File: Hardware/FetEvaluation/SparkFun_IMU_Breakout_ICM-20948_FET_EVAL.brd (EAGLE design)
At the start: 25.4 x 25.4 mm, 102 parts, among them Q1 DMN2005LP4K-7, Q10 RE1C002UN, Q11 DMN2005LP4K-7, Q12 RE1C002UN, Q13 DMN2005LP4K-7, Q14 RE1C002UN, Q15 DMN2005LP4K-7, Q16 RE1C002UN, Q2 RE1C002UN, Q3 DMN2005LP4K-7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

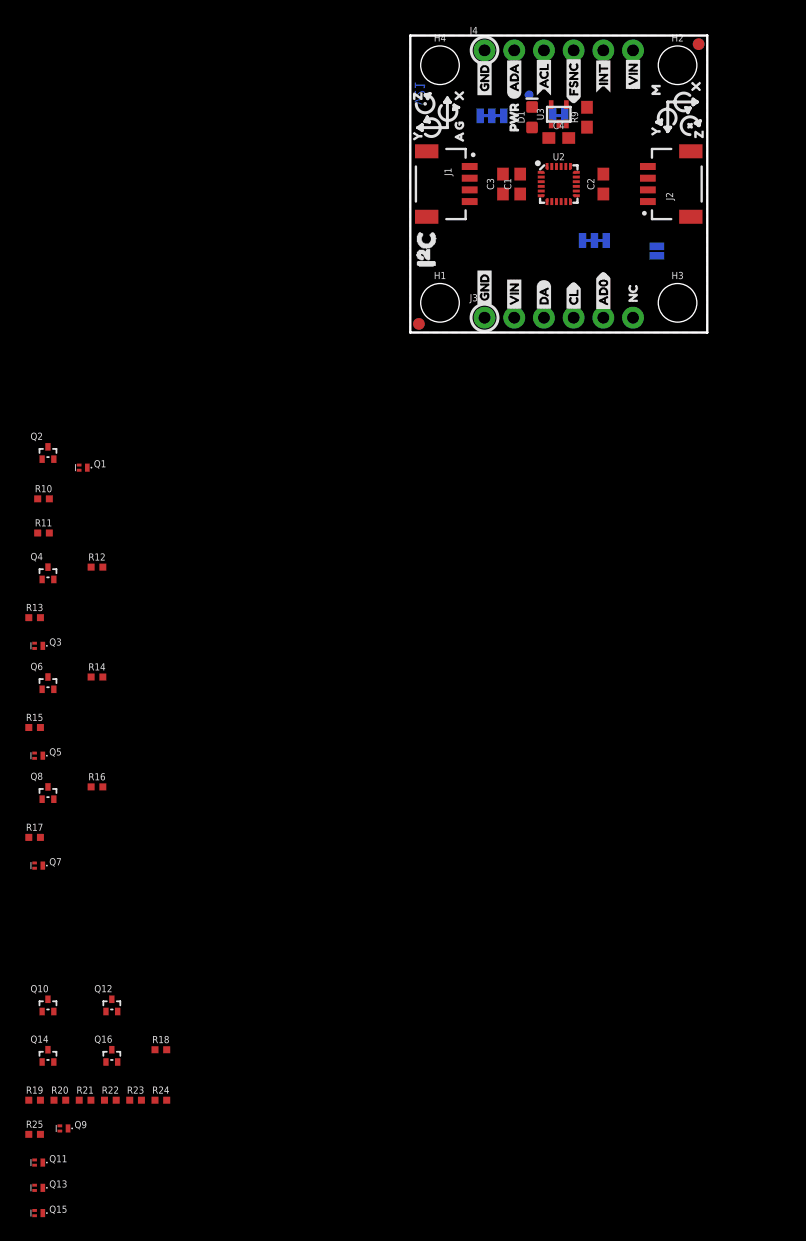
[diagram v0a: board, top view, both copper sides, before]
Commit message: Laid out board for MOSFET trick evaluation (prototype)
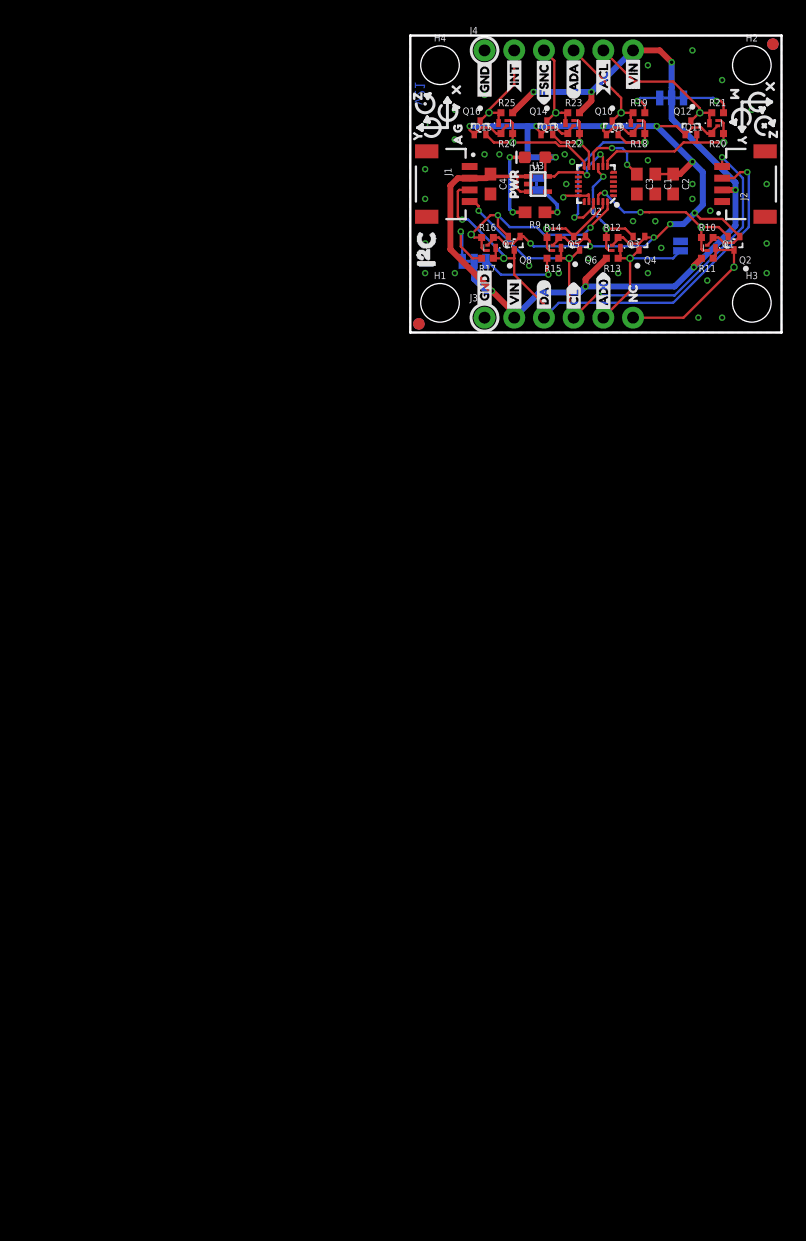
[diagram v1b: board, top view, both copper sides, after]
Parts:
- added U1, U10, U11, U12, U13, U14, U15, U16, U17, U18, U4, U5, U6, U7, U8, U9: TP, new_fets:MINI_TEST_POINT
- moved Q11 106.4 mm to (26.3, 17.9), turned to 180 degrees
- moved Q13 102.1 mm to (14.0, 17.9), turned to 180 degrees
- moved Q15 101.6 mm to (8.26, 17.9), turned to 180 degrees
- moved R21 100.3 mm to (26.3, 18.8)
- moved R20 100.0 mm to (26.3, 17.0), turned to 180 degrees
- moved Q9 99.2 mm to (19.6, 17.9), turned to 180 degrees
- moved R19 99.0 mm to (19.6, 18.8)
- moved R25 96.3 mm to (8.26, 18.8)
- moved R23 92.4 mm to (14.0, 18.8)
- moved R22 91.7 mm to (14.0, 17.0), turned to 180 degrees
- moved Q14 90.1 mm to (11.7, 18.0)
- moved Q12 89.9 mm to (24.0, 18.0)
- moved Q10 89.2 mm to (17.3, 18.0)
- moved R18 88.4 mm to (19.6, 17.0), turned to 180 degrees
- moved R24 87.8 mm to (8.26, 17.0), turned to 180 degrees
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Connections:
- net !CS: now also U17.P$1
- net !CS!_VIN: now also U18.P$1
- net AD0/SDO: now also U15.P$1
- net AD0/SDO_VIN: now also U16.P$1
- net AUX_CL: now also U5.P$1
- net AUX_CL_VIN: now also J4.5, U6.P$1; no longer J4.3
- net AUX_DA: now also U1.P$1
- net AUX_DA_VIN: now also J4.4, U4.P$1; no longer J4.2
- net FSYNC: now also U8.P$1
- net FSYNC_VIN: now also J4.3, U7.P$1; no longer J4.4
- net INT: now also U9.P$1
- net INT_VIN: now also J4.2, U10.P$1; no longer J4.5
- net SCL/SCLK: now also U13.P$1
- net SCL/SCLK_VIN: now also U14.P$1
- net SDA/SDI: now also U11.P$1
- net SDA/SDI_VIN: now also U12.P$1
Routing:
- net 1.8V: track 0.00 -> 100.8 mm, vias 0 -> 13
- net VIN: track 0.00 -> 88.5 mm, vias 0 -> 7
- net SDA/SDI_VIN: track 0.00 -> 46.5 mm, vias 0 -> 2
- net SCL/SCLK_VIN: track 0.00 -> 44.2 mm, vias 0 -> 3
- net SDA/SDI: track 0.00 -> 19.3 mm, vias 0 -> 2
- net AUX_DA: track 0.00 -> 18.4 mm, vias 0 -> 1
- net !CS: track 0.00 -> 15.7 mm, vias 0 -> 2
- net !CS!_VIN: track 0.00 -> 14.5 mm
- net AUX_CL: track 0.00 -> 14.0 mm
- net AUX_CL_VIN: track 0.00 -> 13.7 mm
- net AD0/SDO_VIN: track 0.00 -> 13.7 mm
- net INT: track 0.00 -> 12.0 mm
- net AD0/SDO: track 0.00 -> 11.2 mm, vias 0 -> 1
- net AUX_DA_VIN: track 0.00 -> 10.1 mm
- net INT_VIN: track 0.00 -> 9.28 mm
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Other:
- board size 25.4 x 25.4 mm -> 31.8 x 25.4 mm

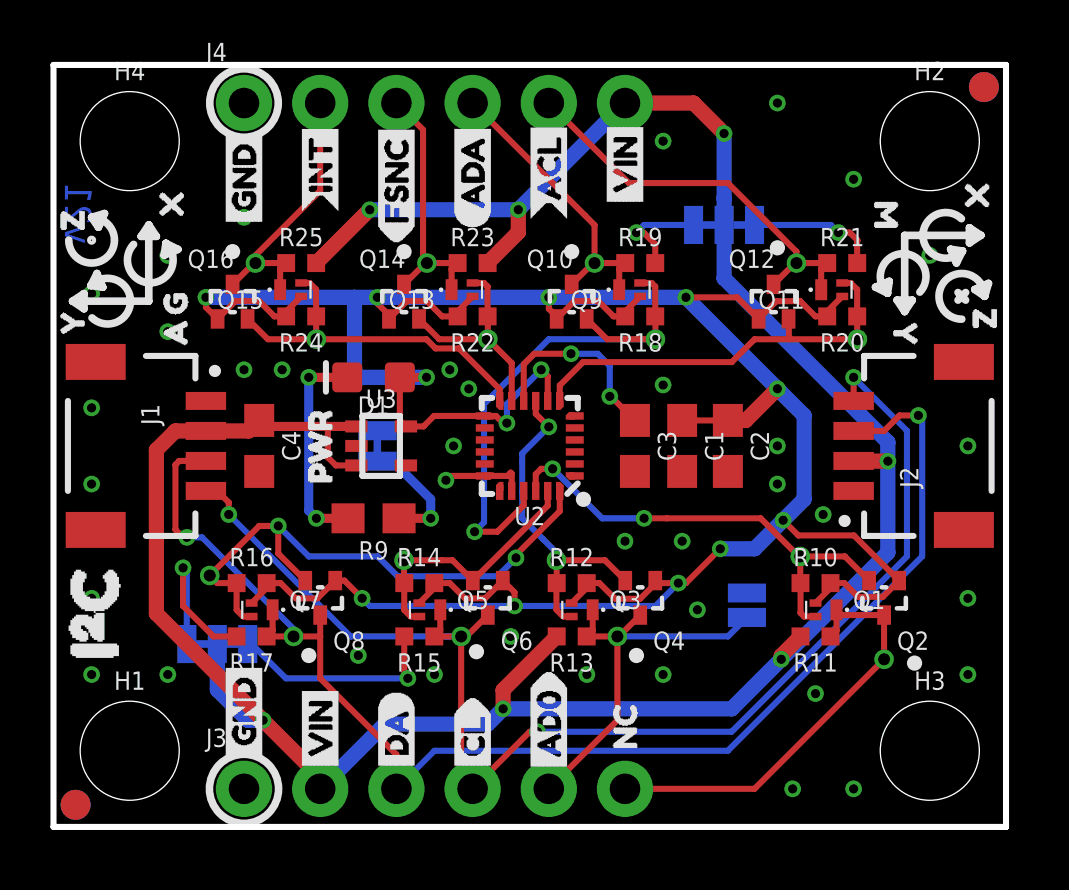
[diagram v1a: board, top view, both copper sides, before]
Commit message: Updated test point package with keepout
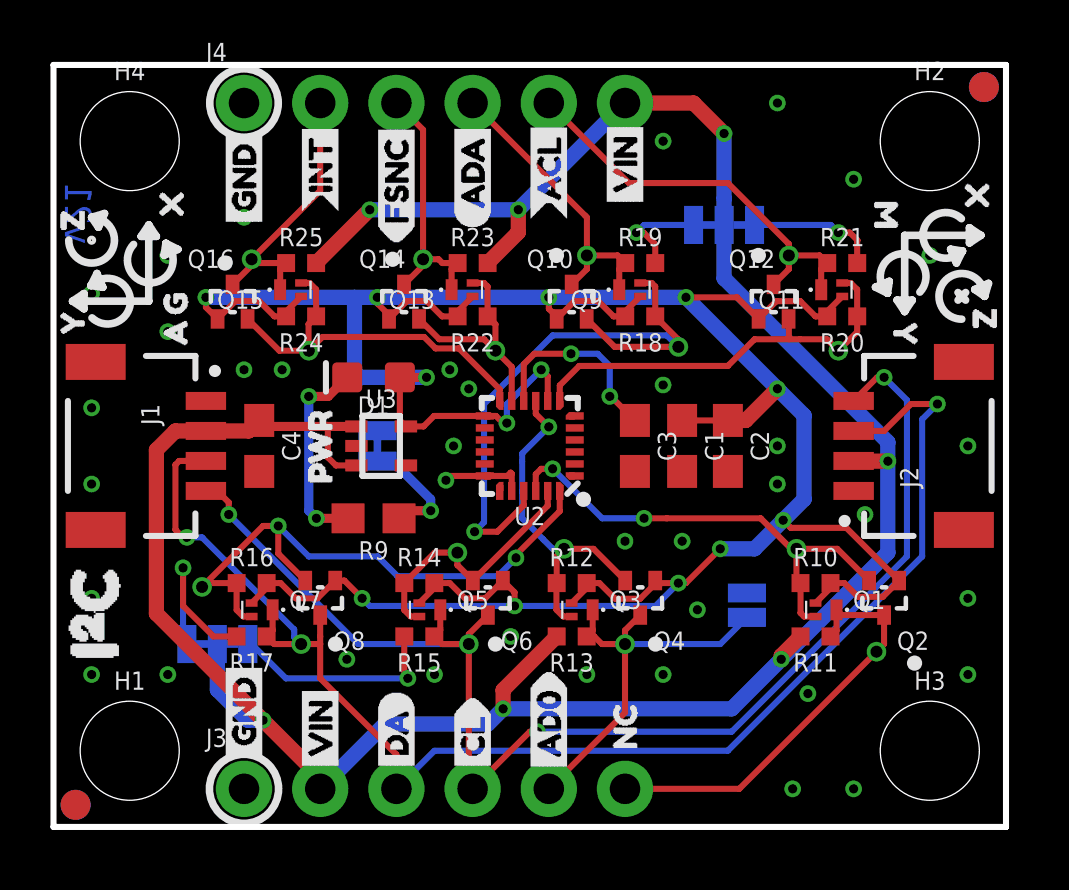
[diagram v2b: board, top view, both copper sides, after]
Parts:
- moved U13 1.80 mm to (13.5, 9.14)
- moved U1 0.80 mm to (20.8, 16.0)
- moved U5 0.74 mm to (26.2, 15.9)
- moved U15 0.46 mm to (17.0, 9.27)
- moved U11 0.46 mm to (4.95, 8.00)
- moved U8 0.46 mm to (14.7, 15.9)
- moved U9 0.46 mm to (8.51, 15.9)
- moved U6 0.36 mm to (24.5, 19.1)
- moved U12 0.36 mm to (8.26, 6.10)
- moved U16 0.36 mm to (19.1, 6.10)
- moved U18 0.36 mm to (27.4, 5.84)
- moved U14 0.36 mm to (13.8, 6.10)
- moved U4 0.36 mm to (17.8, 19.1)
- moved U17 0.28 mm to (24.8, 9.27)
- moved U10 0.18 mm to (6.60, 18.9)
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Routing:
- net AUX_DA: track 18.4 -> 20.8 mm
- net SDA/SDI_VIN: track 46.5 -> 48.1 mm
- net INT: track 12.0 -> 12.8 mm
- net SDA/SDI: track 19.3 -> 19.9 mm
- net SCL/SCLK_VIN: track 44.2 -> 44.8 mm

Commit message: Commit for design review
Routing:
- net SDA/SDI_VIN_JMP: track 6.07 -> 4.76 mm
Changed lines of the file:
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@@
 <contactref element="R17" pad="2"/>
 <contactref element="JP4" pad="1"/>
-<wire x1="4.318" y1="7.366" x2="5.334" y2="6.35" width="0.2032" layer="1"/>
-<via x="4.318" y="8.636" extent="1-16" drill="0.3048"/>
-<wire x1="4.318" y1="8.636" x2="4.318" y2="6.223" width="0.2032" layer="16"/>
-<wire x1="4.318" y1="8.636" x2="4.318" y2="7.366" width="0.2032" layer="1"/>
+<wire x1="4.064" y1="7.62" x2="5.334" y2="6.35" width="0.2032" layer="1"/>
+<via x="4.064" y="7.874" extent="1-16" drill="0.3048"/>
+<wire x1="4.064" y1="7.874" x2="4.064" y2="6.858" width="0.2032" layer="16"/>
+<wire x1="4.064" y1="7.874" x2="4.064" y2="7.62" width="0.2032" layer="1"/>
 <wire x1="5.334" y1="6.35" x2="6.104" y2="6.35" width="0.2032" layer="1"/>
-<wire x1="4.318" y1="6.223" x2="4.445" y2="6.096" width="0.2032" layer="16"/>
+<wire x1="4.064" y1="6.858" x2="4.445" y2="6.477" width="0.2032" layer="16"/>
+<wire x1="4.445" y1="6.477" x2="4.445" y2="6.096" width="0.2032" layer="16"/>
 </signal>
 <signal name="SCL/SCLK_VIN_JMP">

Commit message: Move CC block, ready for proto review
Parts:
- moved FRAME2 39.4 mm to (-5.71, -15.6)
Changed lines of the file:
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@@
 <setting verticaltext="up"/>
 </settings>
-<grid distance="5" unitdist="mil" unit="mil" style="lines" multiple="1" display="yes" altdistance="0.005" altunitdist="inch" altunit="inch"/>
+<grid distance="5" unitdist="mil" unit="mil" style="lines" multiple="1" display="yes" altdistance="1" altunitdist="mil" altunit="mil"/>
 <layers>
 <layer number="1" name="Top" color="4" fill="1" visible="yes" active="yes"/>
@@
 <layer number="37" name="tTest" color="7" fill="1" visible="no" active="yes"/>
 <layer number="38" name="bTest" color="7" fill="1" visible="no" active="yes"/>
-<layer number="39" name="tKeepout" color="4" fill="11" visible="yes" active="yes"/>
+<layer number="39" name="tKeepout" color="4" fill="11" visible="no" active="yes"/>
 <layer number="40" name="bKeepout" color="1" fill="11" visible="no" active="yes"/>
 <layer number="41" name="tRestrict" color="4" fill="10" visible="no" active="yes"/>
@@
 <layer number="43" name="vRestrict" color="2" fill="10" visible="no" active="yes"/>
 <layer number="44" name="Drills" color="7" fill="1" visible="no" active="yes"/>
-<layer number="45" name="Holes" color="7" fill="1" visible="no" active="yes"/>
+<layer number="45" name="Holes" color="7" fill="1" visible="yes" active="yes"/>
 <layer number="46" name="Milling" color="3" fill="1" visible="no" active="yes"/>
 <layer number="47" name="Measures" color="7" fill="1" visible="no" active="yes"/>
@@
 <layer number="49" name="Reference" color="7" fill="1" visible="no" active="yes"/>
 <layer number="50" name="dxf" color="7" fill="1" visible="no" active="yes"/>
-<layer number="51" name="tDocu" color="6" fill="1" visible="no" active="yes"/>
-<layer number="52" name="bDocu" color="7" fill="1" visible="no" active="yes"/>
+<layer number="51" name="tDocu" color="6" fill="1" visible="yes" active="yes"/>
+<layer number="52" name="bDocu" color="7" fill="1" visible="yes" active="yes"/>
 <layer number="91" name="Nets" color="2" fill="1" visible="no" active="no"/>
 <layer number="92" name="Busses" color="1" fill="1" visible="no" active="no"/>
@@
 <wire x1="31.75" y1="0" x2="0" y2="0" width="0.2032" layer="20"/>
 <text x="0.381" y="19.431" size="0.889" layer="16" font="vector" ratio="20" rot="SMR90">v21</text>
-<text x="20.465" y="-9.795" size="1.778" layer="51" font="vector" ratio="15">Owen Lyke</text>
+<text x="22.37" y="-15.764" size="1.778" layer="51" font="vector" ratio="15">Owen Lyke</text>
 <circle x="6.35" y="24.13" radius="1.141021875" width="0.254" layer="21"/>
 <circle x="6.35" y="1.27" radius="1.15199375" width="0.254" layer="21"/>
@@
 <attribute name="PROD_ID" value="RES-14341" x="10.414" y="7.112" size="1.778" layer="27" font="vector" ratio="15" rot="R180" display="off"/>
 </element>
-<element name="FRAME2" library="SparkFun-Aesthetics" package="CREATIVE_COMMONS" value="FRAME-LEDGER" x="-12.319" y="-54.483">
-<attribute name="DESIGNER" value="Owen Lyke" x="-12.319" y="-54.483" size="1.778" layer="27" font="vector" ratio="15" display="off"/>
-<attribute name="REV" value="v21" x="-12.319" y="-54.483" size="1.778" layer="27" font="vector" ratio="15" display="off"/>
+<element name="FRAME2" library="SparkFun-Aesthetics" package="CREATIVE_COMMONS" value="FRAME-LEDGER" x="-5.715" y="-15.621">
+<attribute name="DESIGNER" value="Owen Lyke" x="-5.715" y="-15.621" size="1.778" layer="27" font="vector" ratio="15" display="off"/>
+<attribute name="REV" value="v21" x="-5.715" y="-15.621" size="1.778" layer="27" font="vector" ratio="15" display="off"/>
 </element>
 <element name="Q9" library="new_fets" package="AP02001" value="DMN2005LP4K-7" x="19.558" y="17.907" rot="R180"/>
